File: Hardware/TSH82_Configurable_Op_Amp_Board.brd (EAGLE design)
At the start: 160 x 100 mm, 33 parts, among them U1 TSH82

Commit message: Close to done, labels, layout, etc.
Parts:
- added FD1, FD2: FIDUCIAL1X2, SparkFun-Aesthetics:FIDUCIAL-1X2
- added H1, H2: STAND-OFF, SparkFun-Hardware:STAND-OFF
- added LOGO1: SFE_LOGO_NAME_FLAME.2_INCH, SparkFun-Aesthetics:SFE_LOGO_NAME_FLAME_.2
- added U$1: (no value), buzzard_labels:VREF9
- added U$2: (no value), buzzard_labels:#VEE2
- added U$3: (no value), buzzard_labels:#VCC1
- added U$4: (no value), buzzard_labels:#IN13
- added U$5: (no value), buzzard_labels:#IN14
- added U$6: (no value), buzzard_labels:OUT15
- added U$7: (no value), buzzard_labels:#IN26
- added U$8: (no value), buzzard_labels:#IN27
- added U$9: (no value), buzzard_labels:OUT28
- moved FRAME1 72.0 mm to (-8.89, -10.2)
- moved C7 68.0 mm to (8.89, 8.64), turned to 90 degrees
- moved C6 66.8 mm to (11.4, 8.64), turned to 90 degrees
- moved JP5 61.8 mm to (11.4, 8.89), flipped to the bottom, turned to 270 degrees
- moved JP8 60.4 mm to (16.5, 8.89), flipped to the bottom, turned to 270 degrees
- moved JP10 54.8 mm to (21.6, 12.1), flipped to the bottom, turned to 90 degrees
- moved JP2 54.2 mm to (8.48, 12.7), flipped to the bottom, turned to 90 degrees
- moved JP4 52.0 mm to (16.1, 12.7), flipped to the bottom, turned to 90 degrees
- moved JP7 51.8 mm to (19.1, 8.89), flipped to the bottom, turned to 270 degrees
- moved C2 46.5 mm to (4.19, 16.6)
- moved C9 46.2 mm to (16.5, 8.64), turned to 90 degrees
- moved C10 45.5 mm to (14.8, 12.6), turned to 180 degrees
- moved C8 45.2 mm to (19.1, 8.64), turned to 90 degrees
- moved R2 44.8 mm to (5.54, 11.4), turned to 180 degrees
- moved JP1 41.5 mm to (11.0, 12.7), flipped to the bottom, turned to 270 degrees
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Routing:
- net VREF: track 0.00 -> 47.1 mm, vias 0 -> 1
- net VCC: track 0.00 -> 42.0 mm
- net VNEG: track 0.00 -> 34.8 mm, vias 0 -> 2
- net OUT1: track 0.00 -> 23.2 mm, vias 0 -> 1
- net OUT2: track 0.00 -> 22.3 mm
- net -IN2: track 0.00 -> 8.40 mm, vias 0 -> 1
- net -IN1: track 0.00 -> 8.40 mm, vias 0 -> 1
- net +IN2: track 0.00 -> 8.40 mm, vias 0 -> 1
- net +IN1: track 0.00 -> 8.40 mm, vias 0 -> 1
- net N$4: track 0.00 -> 7.93 mm, vias 0 -> 1
- net N$16: track 0.00 -> 6.93 mm, vias 0 -> 1
- net N$1: track 0.00 -> 6.13 mm
- net N$2: track 0.00 -> 5.76 mm
- net N$11: track 0.00 -> 5.62 mm
- net N$9: track 0.00 -> 4.18 mm, vias 0 -> 1
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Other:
- board size 160 x 100 mm -> 22.8 x 26.3 mm

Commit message: Ready for review.
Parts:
- removed FD1, FD2: FIDUCIAL1X2, SparkFun-Aesthetics:FIDUCIAL-1X2
- added LOGO2: SFE_LOGO_NAME_FLAME.1_INCH, SparkFun-Aesthetics:SFE_LOGO_NAME_FLAME_.1
- added LOGO3: OSHW-LOGOS, SparkFun-Aesthetics:OSHW-LOGO-S
- added U$10, U$11: (no value), buzzard_labels (5):OUT17
- added U$12, U$13: (no value), buzzard_labels (5):#IN24
- added U$14, U$16: (no value), buzzard_labels (5):#IN25
- added U$15, U$17: (no value), buzzard_labels (5):OUT28
- added U$22, U$26: (no value), buzzard_labels (4):TSH820
- added U$23, U$27: (no value), buzzard_labels (4):CONFIGURABLE1
- added U$24, U$28: (no value), buzzard_labels (4):OPAMP2
- added U$25, U$29: (no value), buzzard_labels (4):BOARD3
- added U$30: (no value), buzzard_labels (5):#VCC0
- LOGO1: value SFE_LOGO_NAME_FLAME.2_INCH -> SFE_LOGO_FLAME.2_INCH; device SparkFun-Aesthetics:SFE_LOGO_NAME_FLAME_.2 -> SparkFun-Aesthetics:SFE_LOGO_FLAME_.2
- U$1: device buzzard_labels:VREF9 -> buzzard_labels (5):#VEE1
- U$2: device buzzard_labels:#VEE2 -> buzzard_labels (5):#VEE1
- U$3: device buzzard_labels:#VCC1 -> buzzard_labels (5):#VCC0
- U$4: device buzzard_labels:#IN13 -> buzzard_labels (5):VREF6
- U$5: device buzzard_labels:#IN14 -> buzzard_labels (5):VREF6
- U$6: device buzzard_labels:OUT15 -> buzzard_labels (5):#IN12
- U$7: device buzzard_labels:#IN26 -> buzzard_labels (5):#IN12
- U$8: device buzzard_labels:#IN27 -> buzzard_labels (5):#IN13
- U$9: device buzzard_labels:OUT28 -> buzzard_labels (5):#IN13
- moved LOGO1 21.5 mm to (4.22, 19.7), flipped to the top
- moved U$9 10.1 mm to (11.4, 2.21), flipped to the bottom
- moved U$8 7.52 mm to (11.4, 2.21)
- moved U$7 7.45 mm to (8.89, 2.21)
- moved U$6 5.04 mm to (8.89, 2.21), flipped to the bottom
- moved U$5 4.86 mm to (6.35, 2.21), flipped to the bottom
- moved U$1 2.49 mm to (3.81, 2.21)
- moved U$4 2.41 mm to (6.35, 2.21)
- moved H1 1.27 mm to (2.54, 22.9)
- moved H2 1.27 mm to (20.3, 22.9)
- moved C5 0.64 mm to (21.4, 17.7)
- moved C7 0.64 mm to (8.79, 9.27)
- moved C8 0.64 mm to (18.9, 9.27)
- moved C9 0.64 mm to (16.4, 9.27)
- moved R3 0.64 mm to (9.02, 16.8)
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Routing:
- net VREF: track 47.1 -> 47.8 mm
- net OUT2: track 22.3 -> 22.9 mm
- net -IN2: track 8.40 -> 9.07 mm
- net -IN1: track 8.40 -> 9.07 mm
- net +IN2: track 8.40 -> 9.07 mm
- net +IN1: track 8.40 -> 9.07 mm
- net OUT1: track 23.2 -> 23.9 mm
- net VNEG: track 34.8 -> 35.3 mm, vias 2 -> 7
- net VCC: track 42.0 -> 42.6 mm
- added copper zone on layer 1, net VNEG
- added copper zone on layer 16, net VNEG
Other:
- board size 22.8 x 26.3 mm -> 22.9 x 25.4 mm
- board text added: "JP1"
- board text added: "JP10"
- board text added: "JP2"
- board text added: "JP3"
- board text added: "JP4"
- board text added: "JP5"
- board text added: "JP6"
- board text added: "JP7"
- board text added: "JP8"
- board text added: "JP9"
- board text added: "Pete Dokter"
- board text added: "v01"

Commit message: Changes post design review.
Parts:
- added FD1, FD2: FIDUCIALUFIDUCIAL, SparkFun-Aesthetics:FIDUCIAL-MICRO
- added U$18: (no value), buzzard_labels (6):JP10
- added U$19: (no value), buzzard_labels (6):JP21
- added U$20: (no value), buzzard_labels (6):JP32
- added U$21: (no value), buzzard_labels (6):JP43
- added U$31: (no value), buzzard_labels (6):JP54
- added U$32: (no value), buzzard_labels (6):JP65
- added U$33: (no value), buzzard_labels (6):JP76
- added U$34: (no value), buzzard_labels (6):JP87
- added U$35: (no value), buzzard_labels (6):JP98
- added U$36: (no value), buzzard_labels (6):JP109
- J1: device SparkFun-Connectors:1X09 -> SparkFun-Connectors:1X09_NO_SILK
- moved U$1 0.79 mm to (3.84, 1.42)
- moved U$2 0.79 mm to (3.84, 1.42)
- moved U$10 0.79 mm to (14.0, 1.42)
- moved U$11 0.79 mm to (14.0, 1.42)
- moved U$4 0.79 mm to (6.35, 1.42)
- moved U$5 0.79 mm to (6.35, 1.42)
- moved U$15 0.76 mm to (21.6, 1.45)
- moved U$17 0.76 mm to (21.6, 1.45)
- moved U$6 0.74 mm to (8.92, 1.47)
- moved U$7 0.74 mm to (8.92, 1.47)
- moved U$12 0.74 mm to (16.5, 1.47)
- moved U$13 0.74 mm to (16.5, 1.47)
- moved U$14 0.74 mm to (19.1, 1.47)
- moved U$16 0.74 mm to (19.1, 1.47)
- moved U$3 0.74 mm to (1.27, 1.47)
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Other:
- board text removed: "JP1"
- board text removed: "JP10"
- board text removed: "JP2"
- board text removed: "JP3"
- board text removed: "JP4"
- board text removed: "JP5"
- board text removed: "JP6"
- board text removed: "JP7"
- board text removed: "JP8"
- board text removed: "JP9"
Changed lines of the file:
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@@
 <grid distance="50" unitdist="mil" unit="mil" style="dots" multiple="1" display="yes" altdistance="1" altunitdist="mil" altunit="mil"/>
 <layers>
-<layer number="1" name="Top" color="4" fill="1" visible="yes" active="yes"/>
+<layer number="1" name="Top" color="4" fill="1" visible="no" active="yes"/>
 <layer number="2" name="Route2" color="1" fill="3" visible="no" active="no"/>
 <layer number="15" name="Route15" color="4" fill="6" visible="no" active="no"/>
@@
 <layer number="19" name="Unrouted" color="6" fill="1" visible="yes" active="yes"/>
 <layer number="20" name="Dimension" color="24" fill="1" visible="yes" active="yes"/>
-<layer number="21" name="tPlace" color="7" fill="1" visible="yes" active="yes"/>
+<layer number="21" name="tPlace" color="7" fill="1" visible="no" active="yes"/>
 <layer number="22" name="bPlace" color="7" fill="1" visible="yes" active="yes"/>
-<layer number="23" name="tOrigins" color="15" fill="1" visible="yes" active="yes"/>
+<layer number="23" name="tOrigins" color="15" fill="1" visible="no" active="yes"/>
 <layer number="24" name="bOrigins" color="15" fill="1" visible="yes" active="yes"/>
 <layer number="25" name="tNames" color="7" fill="1" visible="no" active="yes"/>
@@
 <layer number="49" name="Reference" color="7" fill="1" visible="yes" active="yes"/>
 <layer number="50" name="dxf" color="7" fill="1" visible="no" active="no"/>
-<layer number="51" name="tDocu" color="7" fill="1" visible="yes" active="yes"/>
+<layer number="51" name="tDocu" color="7" fill="1" visible="no" active="yes"/>
 <layer number="52" name="bDocu" color="7" fill="1" visible="no" active="yes"/>
 <layer number="53" name="tGND_GNDA" color="7" fill="9" visible="no" active="no"/>
@@
 <wire x1="22.86" y1="25.4" x2="0" y2="25.4" width="0.2032" layer="20"/>
 <wire x1="0" y1="25.4" x2="0" y2="0" width="0.2032" layer="20"/>
-<text x="11.8364" y="15.2146" size="0.8128" layer="22" font="vector" ratio="15" rot="MR0">JP1</text>
-<text x="9.2964" y="15.2146" size="0.8128" layer="22" font="vector" ratio="15" rot="MR0">JP2</text>
-<text x="19.4564" y="15.2146" size="0.8128" layer="22" font="vector" ratio="15" rot="MR0">JP3</text>
-<text x="16.9418" y="15.2146" size="0.8128" layer="22" font="vector" ratio="15" rot="MR0">JP4</text>
-<text x="12.3444" y="7.4422" size="0.8128" layer="22" font="vector" ratio="15" rot="MR0">JP5</text>
-<text x="9.8044" y="7.4422" size="0.8128" layer="22" font="vector" ratio="15" rot="MR0">JP6</text>
-<text x="19.9644" y="7.4422" size="0.8128" layer="22" font="vector" ratio="15" rot="MR0">JP7</text>
-<text x="17.399" y="7.4422" size="0.8128" layer="22" font="vector" ratio="15" rot="MR0">JP8</text>
-<text x="6.7564" y="13.9446" size="0.8128" layer="22" font="vector" ratio="15" rot="MR0">JP9</text>
-<text x="22.6822" y="13.97" size="0.8128" layer="22" font="vector" ratio="15" rot="MR0">JP10</text>
 <text x="0.3048" y="13.3604" size="0.8128" layer="16" font="vector" ratio="15" rot="MR90">v01</text>
 <text x="17.78" y="-10.16" size="1.778" layer="51" font="vector">Pete Dokter</text>
@@
 </element>
 <element name="FRAME1" library="SparkFun-Aesthetics" package="CREATIVE_COMMONS" value="FRAME-LETTER" x="-8.89" y="-10.16"/>
-<element name="J1" library="SparkFun-Connectors" package="1X09" value="" x="1.27" y="1.27"/>
+<element name="J1" library="SparkFun-Connectors" package="1X09_NO_SILK" value="" x="1.27" y="1.27"/>
 <element name="JP1" library="SparkFun-Jumpers" package="SMT-JUMPER_3_1-NC_TRACE_SILK" value="JUMPER-SMT_3_1-NC_TRACE_SILK" x="10.922" y="13.3604" rot="MR270"/>
 <element name="JP10" library="SparkFun-Jumpers" package="SMT-JUMPER_2_NO_SILK" value="JUMPER-SMT_2_NO_SILK" x="21.463" y="12.7254" rot="MR90"/>
@@
 <element name="U$28" library="buzzard_labels (4)" package="OPAMP2" value="" x="17.8562" y="17.526" rot="MR0"/>
 <element name="U$29" library="buzzard_labels (4)" package="BOARD3" value="" x="11.7856" y="17.526" rot="MR0"/>
-<element name="U$30" library="buzzard_labels (5)" package="#VCC0" value="" x="1.27" y="2.2098" rot="MR90"/>
-<element name="U$1" library="buzzard_labels (5)" package="#VEE1" value="" x="3.81" y="2.2098" rot="R90"/>
-<element name="U$2" library="buzzard_labels (5)" package="#VEE1" value="" x="3.81" y="2.2098" rot="MR90"/>
-<element name="U$3" library="buzzard_labels (5)" package="#VCC0" value="" x="1.27" y="2.2098" rot="R90"/>
-<element name="U$4" library="buzzard_labels (5)" package="VREF6" value="" x="6.35" y="2.2098" rot="R90"/>
-<element name="U$5" library="buzzard_labels (5)" package="VREF6" value="" x="6.35" y="2.2098" rot="MR90"/>
-<element name="U$6" library="buzzard_labels (5)" package="#IN12" value="" x="8.89" y="2.2098" rot="MR90"/>
-<element name="U$7" library="buzzard_labels (5)" package="#IN12" value="" x="8.89" y="2.2098" rot="R90"/>
-<element name="U$8" library="buzzard_labels (5)" package="#IN13" value="" x="11.43" y="2.2098" rot="R90"/>
-<element name="U$9" library="buzzard_labels (5)" package="#IN13" value="" x="11.43" y="2.2098" rot="MR90"/>
-<element name="U$10" library="buzzard_labels (5)" package="OUT17" value="" x="13.97" y="2.2098" rot="R90"/>
-<element name="U$11" library="buzzard_labels (5)" package="OUT17" value="" x="13.97" y="2.2098" rot="MR90"/>
-<element name="U$12" library="buzzard_labels (5)" package="#IN24" value="" x="16.51" y="2.2098" rot="R90"/>
-<element name="U$13" library="buzzard_labels (5)" package="#IN24" value="" x="16.51" y="2.2098" rot="MR90"/>
-<element name="U$14" library="buzzard_labels (5)" package="#IN25" value="" x="19.05" y="2.2098" rot="R90"/>
-<element name="U$16" library="buzzard_labels (5)" package="#IN25" value="" x="19.05" y="2.2098" rot="MR90"/>
-<element name="U$15" library="buzzard_labels (5)" package="OUT28" value="" x="21.59" y="2.2098" rot="R90"/>
-<element name="U$17" library="buzzard_labels (5)" package="OUT28" value="" x="21.59" y="2.2098" rot="MR90"/>
+<element name="U$30" library="buzzard_labels (5)" package="#VCC0" value="" x="1.27" y="1.4732" rot="MR90"/>
+<element name="U$1" library="buzzard_labels (5)" package="#VEE1" value="" x="3.8354" y="1.4224" rot="R90"/>
+<element name="U$2" library="buzzard_labels (5)" package="#VEE1" value="" x="3.8354" y="1.4224" rot="MR90"/>
+<element name="U$3" library="buzzard_labels (5)" package="#VCC0" value="" x="1.27" y="1.4732" rot="R90"/>
+<element name="U$4" library="buzzard_labels (5)" package="VREF6" value="" x="6.35" y="1.4224" rot="R90"/>
+<element name="U$5" library="buzzard_labels (5)" package="VREF6" value="" x="6.35" y="1.4224" rot="MR90"/>
+<element name="U$6" library="buzzard_labels (5)" package="#IN12" value="" x="8.9154" y="1.4732" rot="MR90"/>
+<element name="U$7" library="buzzard_labels (5)" package="#IN12" value="" x="8.9154" y="1.4732" rot="R90"/>
+<element name="U$8" library="buzzard_labels (5)" package="#IN13" value="" x="11.43" y="1.4732" rot="R90"/>
+<element name="U$9" library="buzzard_labels (5)" package="#IN13" value="" x="11.43" y="1.4732" rot="MR90"/>
+<element name="U$10" library="buzzard_labels (5)" package="OUT17" value="" x="13.97" y="1.4224" rot="R90"/>
+<element name="U$11" library="buzzard_labels (5)" package="OUT17" value="" x="13.97" y="1.4224" rot="MR90"/>
+<element name="U$12" library="buzzard_labels (5)" package="#IN24" value="" x="16.51" y="1.4732" rot="R90"/>
+<element name="U$13" library="buzzard_labels (5)" package="#IN24" value="" x="16.51" y="1.4732" rot="MR90"/>
+<element name="U$14" library="buzzard_labels (5)" package="#IN25" value="" x="19.05" y="1.4732" rot="R90"/>
+<element name="U$16" library="buzzard_labels (5)" package="#IN25" value="" x="19.05" y="1.4732" rot="MR90"/>
+<element name="U$15" library="buzzard_labels (5)" package="OUT28" value="" x="21.59" y="1.4478" rot="R90"/>
+<element name="U$17" library="buzzard_labels (5)" package="OUT28" value="" x="21.59" y="1.4478" rot="MR90"/>
 <element name="LOGO3" library="SparkFun-Aesthetics" package="OSHW-LOGO-S" value="OSHW-LOGOS" x="2.2352" y="19.2532"/>
+<element name="FD1" library="SparkFun-Aesthetics" package="FIDUCIAL-MICRO" value="FIDUCIALUFIDUCIAL" x="21.59" y="20.32"/>
+<element name="FD2" library="SparkFun-Aesthetics" package="FIDUCIAL-MICRO" value="FIDUCIALUFIDUCIAL" x="0.9144" y="8.0264"/>
+<element name="U$18" library="buzzard_labels (6)" package="JP10" value="" x="12.3952" y="15.6464" rot="MR0"/>
+<element name="U$19" library="buzzard_labels (6)" package="JP21" value="" x="9.9314" y="15.6464" rot="MR0"/>
+<element name="U$20" library="buzzard_labels (6)" package="JP32" value="" x="20.0914" y="15.6464" rot="MR0"/>
+<element name="U$21" library="buzzard_labels (6)" package="JP43" value="" x="17.526" y="15.6464" rot="MR0"/>
+<element name="U$31" library="buzzard_labels (6)" package="JP54" value="" x="12.827" y="7.9502" rot="MR0"/>
+<element name="U$32" library="buzzard_labels (6)" package="JP65" value="" x="10.3124" y="7.9502" rot="MR0"/>
+<element name="U$33" library="buzzard_labels (6)" package="JP76" value="" x="20.4724" y="7.9502" rot="MR0"/>
+<element name="U$34" library="buzzard_labels (6)" package="JP87" value="" x="17.907" y="7.9502" rot="MR0"/>
+<element name="U$35" library="buzzard_labels (6)" package="JP98" value="" x="7.3914" y="14.3764" rot="MR0"/>
+<element name="U$36" library="buzzard_labels (6)" package="JP109" value="" x="23.2664" y="14.859" rot="MR0"/>
 </elements>
 <signals>
@@
 <wire x1="6.2856" y1="12.065" x2="6.2856" y2="12.5358" width="0.4064" layer="1"/>
 <wire x1="6.2856" y1="12.5358" x2="5.2324" y2="13.589" width="0.4064" layer="1"/>
-<polygon width="0.254" layer="16" isolate="0.381" orphans="yes">
+<polygon width="0.254" layer="16" isolate="0.381">
 <vertex x="0" y="0"/>
 <vertex x="22.86" y="0"/>

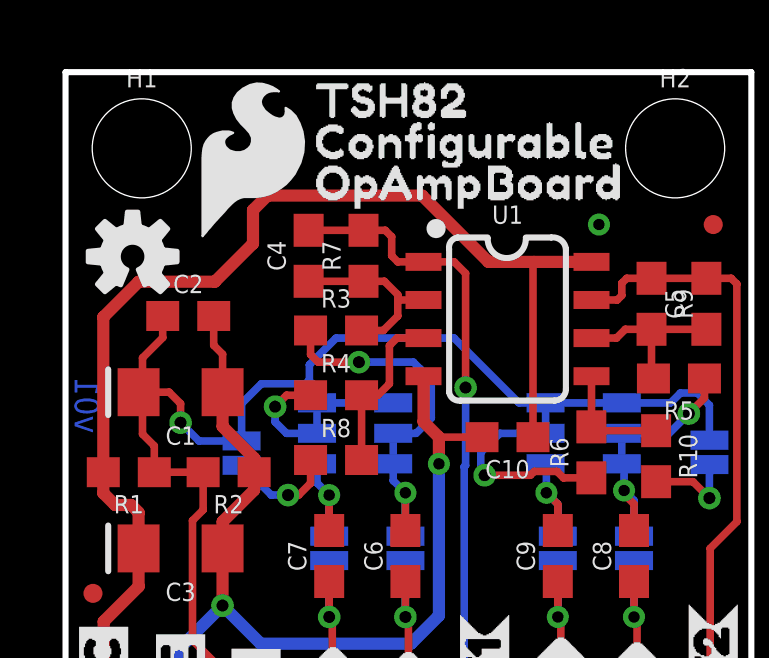
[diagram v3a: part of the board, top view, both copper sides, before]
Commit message: Pushed the power trace out a bit and added some ground vias.
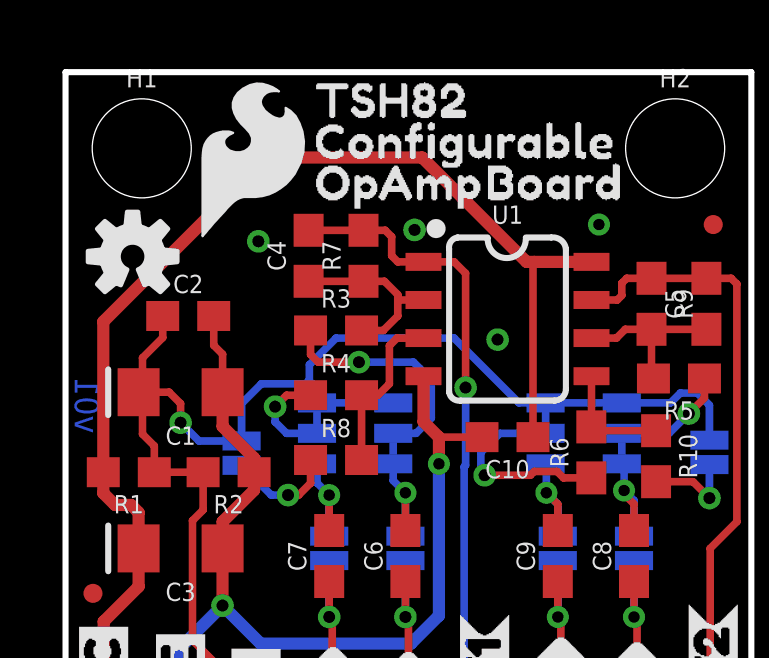
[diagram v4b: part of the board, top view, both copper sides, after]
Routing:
- net VNEG: vias 7 -> 10
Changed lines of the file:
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@@
 <grid distance="50" unitdist="mil" unit="mil" style="dots" multiple="1" display="yes" altdistance="1" altunitdist="mil" altunit="mil"/>
 <layers>
-<layer number="1" name="Top" color="4" fill="1" visible="no" active="yes"/>
+<layer number="1" name="Top" color="4" fill="1" visible="yes" active="yes"/>
 <layer number="2" name="Route2" color="1" fill="3" visible="no" active="no"/>
 <layer number="15" name="Route15" color="4" fill="6" visible="no" active="no"/>
@@
 <layer number="19" name="Unrouted" color="6" fill="1" visible="yes" active="yes"/>
 <layer number="20" name="Dimension" color="24" fill="1" visible="yes" active="yes"/>
-<layer number="21" name="tPlace" color="7" fill="1" visible="no" active="yes"/>
+<layer number="21" name="tPlace" color="7" fill="1" visible="yes" active="yes"/>
 <layer number="22" name="bPlace" color="7" fill="1" visible="yes" active="yes"/>
-<layer number="23" name="tOrigins" color="15" fill="1" visible="no" active="yes"/>
+<layer number="23" name="tOrigins" color="15" fill="1" visible="yes" active="yes"/>
 <layer number="24" name="bOrigins" color="15" fill="1" visible="yes" active="yes"/>
 <layer number="25" name="tNames" color="7" fill="1" visible="no" active="yes"/>
@@
 <layer number="49" name="Reference" color="7" fill="1" visible="yes" active="yes"/>
 <layer number="50" name="dxf" color="7" fill="1" visible="no" active="no"/>
-<layer number="51" name="tDocu" color="7" fill="1" visible="no" active="yes"/>
+<layer number="51" name="tDocu" color="7" fill="1" visible="yes" active="yes"/>
 <layer number="52" name="bDocu" color="7" fill="1" visible="no" active="yes"/>
 <layer number="53" name="tGND_GNDA" color="7" fill="9" visible="no" active="no"/>
@@
 <via x="10.16" y="5.08" extent="1-16" drill="0.381"/>
 <via x="15.24" y="5.08" extent="1-16" drill="0.381"/>
+<via x="6.4262" y="19.7612" extent="1-16" drill="0.4"/>
+<via x="11.6332" y="20.1422" extent="1-16" drill="0.4"/>
+<via x="14.4018" y="16.4846" extent="1-16" drill="0.4"/>
 </signal>
 <signal name="VCC">
@@
 <contactref element="J1" pad="1"/>
 <wire x1="15.582" y1="13.2334" x2="15.582" y2="19.0364" width="0.254" layer="1"/>
-<wire x1="14.097" y1="19.0754" x2="15.621" y2="19.0754" width="0.4064" layer="1"/>
+<wire x1="15.367" y1="19.0754" x2="15.621" y2="19.0754" width="0.4064" layer="1"/>
 <wire x1="15.621" y1="19.0754" x2="17.532" y2="19.0754" width="0.4064" layer="1"/>
 <wire x1="15.582" y1="19.0364" x2="15.621" y2="19.0754" width="0.254" layer="1"/>
@@
 <wire x1="2.1844" y1="10.9728" x2="1.651" y2="10.9728" width="0.4064" layer="1"/>
 <wire x1="2.4354" y1="10.7218" x2="2.1844" y2="10.9728" width="0.4064" layer="1"/>
-<wire x1="1.2582" y1="12.065" x2="1.2582" y2="17.2348" width="0.4064" layer="1"/>
-<wire x1="1.2582" y1="17.2348" x2="2.4384" y2="18.415" width="0.4064" layer="1"/>
-<wire x1="2.4384" y1="18.415" x2="4.9784" y2="18.415" width="0.4064" layer="1"/>
-<wire x1="4.9784" y1="18.415" x2="6.2484" y2="19.685" width="0.4064" layer="1"/>
-<wire x1="6.2484" y1="20.8026" x2="6.731" y2="21.2852" width="0.4064" layer="1"/>
-<wire x1="6.731" y1="21.2852" x2="11.8872" y2="21.2852" width="0.4064" layer="1"/>
-<wire x1="6.2484" y1="19.685" x2="6.2484" y2="20.8026" width="0.4064" layer="1"/>
-<wire x1="11.8872" y1="21.2852" x2="14.097" y2="19.0754" width="0.4064" layer="1"/>
+<wire x1="1.2582" y1="12.065" x2="1.2582" y2="17.0824" width="0.4064" layer="1"/>
+<wire x1="1.2582" y1="17.0824" x2="6.731" y2="22.5552" width="0.4064" layer="1"/>
+<wire x1="6.731" y1="22.5552" x2="11.8872" y2="22.5552" width="0.4064" layer="1"/>
+<wire x1="11.8872" y1="22.5552" x2="15.367" y2="19.0754" width="0.4064" layer="1"/>
 <wire x1="2.4354" y1="8.252" x2="1.27" y2="7.0866" width="0.4064" layer="1"/>
 <wire x1="1.27" y1="7.0866" x2="1.27" y2="1.27" width="0.4064" layer="1"/>
